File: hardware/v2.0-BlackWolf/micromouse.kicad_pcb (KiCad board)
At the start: 2 copper layers, 100 x 74 mm, 106 parts, among them CN1 7_PIN_HEADER, CN2 5_PIN_HEADER, M1 MOTOR_MOUNTS_AND_ENCODERS, M2 LEFT_MOTOR, M3 2.54MM-SLIDE-SWITCH_TS02_SWIT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, M4 RIGHT_MOTOR, P1 B3B-PH-SM4-TB, P2 B3B-PH-SM4-TB, Q1 DMN3150LW, Q2 DMN3150LW, Q3 DMN3150LW, Q4 DMN3150LW, Q5 TEFT4300, Q6 TEFT4300, Q7 TEFT4300, Q8 TEFT4300, SW1 SWITCH_DPST, SW2 SWITCH_DPST, SW3 SWITCH_DPST, U1 STM32F446RE_LQFP64, U10 MPU-9250, U11 TPS76850, U12 TPS73633, U2 MAX14871, U3 MAX14871, U9 HCMS-2901

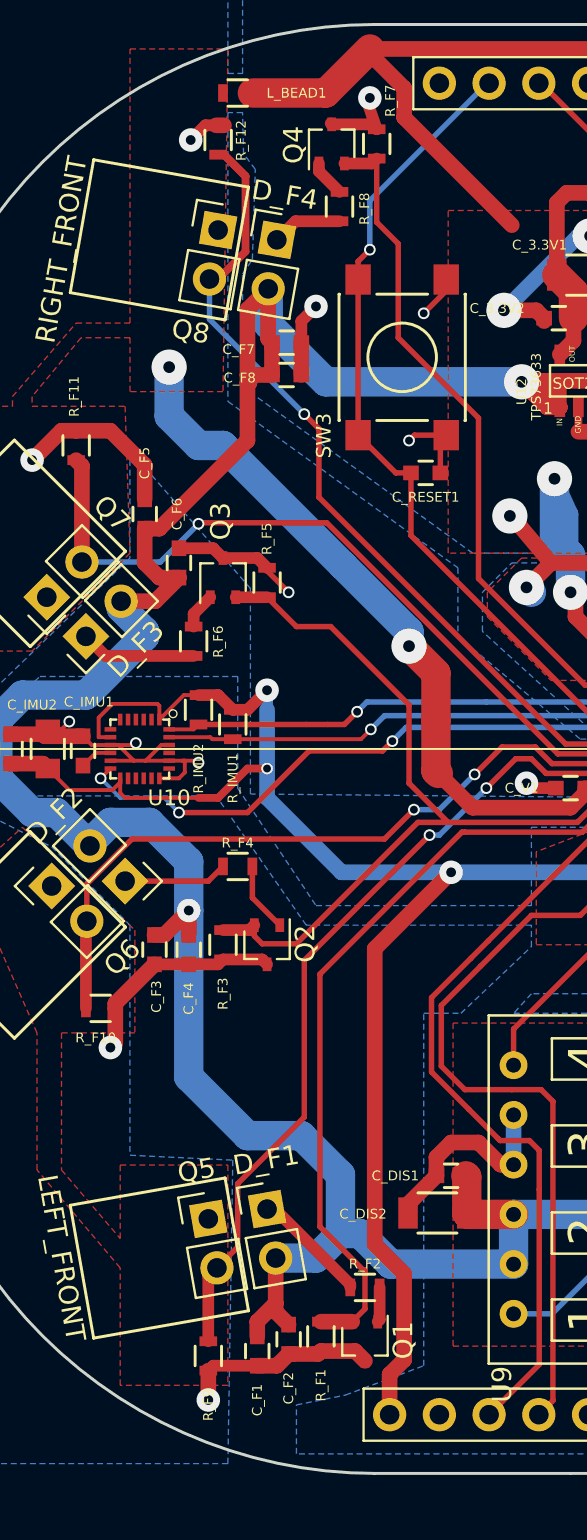
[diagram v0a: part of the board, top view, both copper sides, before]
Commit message: PCB: Fixed wrong NMOS pinmap
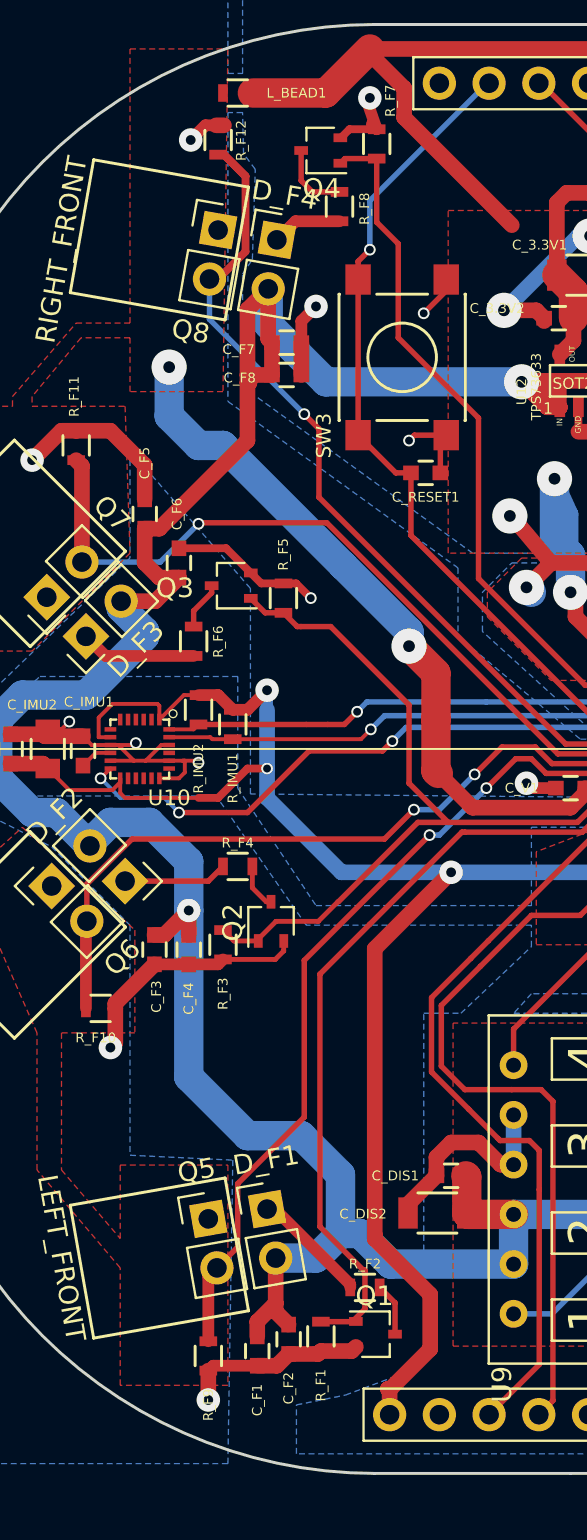
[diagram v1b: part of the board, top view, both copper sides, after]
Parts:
- R_F4, R_F6: value 10 -> 20
- moved Q2 1.21 mm to (155.7, 98.8), turned to 90 degrees
- moved R_F5 1.16 mm to (156.3, 82.3)
- moved Q4 0.65 mm to (158.2, 59.4), turned to 180 degrees
- moved Q1 0.65 mm to (161.0, 119.9), turned to 0 degrees
- moved Q3 0.59 mm to (153.7, 81.7), turned to 180 degrees
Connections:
- Q1 pad 1: Net-(Q1-Pad1) -> EMITTER_FL
- Q1 pad 2: EMITTER_FL -> GND
- Q1 pad 3: GND -> Net-(Q1-Pad3)
- Q2 pad 1: Net-(Q2-Pad1) -> EMITTER_SIDES
- Q2 pad 2: EMITTER_SIDES -> GND
- Q2 pad 3: GND -> Net-(Q2-Pad3)
- Q3 pad 1: Net-(Q3-Pad1) -> EMITTER_SIDES
- Q3 pad 2: EMITTER_SIDES -> GND
- Q3 pad 3: GND -> Net-(Q3-Pad3)
- Q4 pad 1: Net-(Q4-Pad1) -> EMITTER_FR
- Q4 pad 2: EMITTER_FR -> GND
- Q4 pad 3: GND -> Net-(Q4-Pad3)
- R_F2 pad 2: Net-(Q1-Pad1) -> Net-(Q1-Pad3)
- R_F4 pad 2: Net-(Q2-Pad1) -> Net-(Q2-Pad3)
- R_F6 pad 2: Net-(Q3-Pad1) -> Net-(Q3-Pad3)
- R_F8 pad 2: Net-(Q4-Pad1) -> Net-(Q4-Pad3)
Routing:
- net Net-(Q4-Pad3): track 0.00 -> 3.74 mm
- net Net-(Q2-Pad1): track 3.58 -> 0.00 mm
- net Net-(Q1-Pad3): track 0.00 -> 2.71 mm
- net Net-(Q3-Pad3): track 0.00 -> 2.47 mm
- net Net-(Q2-Pad3): track 0.00 -> 2.34 mm
- net GND: track 459.3 -> 461.2 mm
- net Net-(Q4-Pad1): track 1.88 -> 0.00 mm
- net Net-(Q3-Pad1): track 1.85 -> 0.00 mm
- net Net-(Q1-Pad1): track 1.79 -> 0.00 mm
- net EMITTER_SIDES: track 42.8 -> 41.4 mm
- net +3V3: track 286.7 -> 288.1 mm

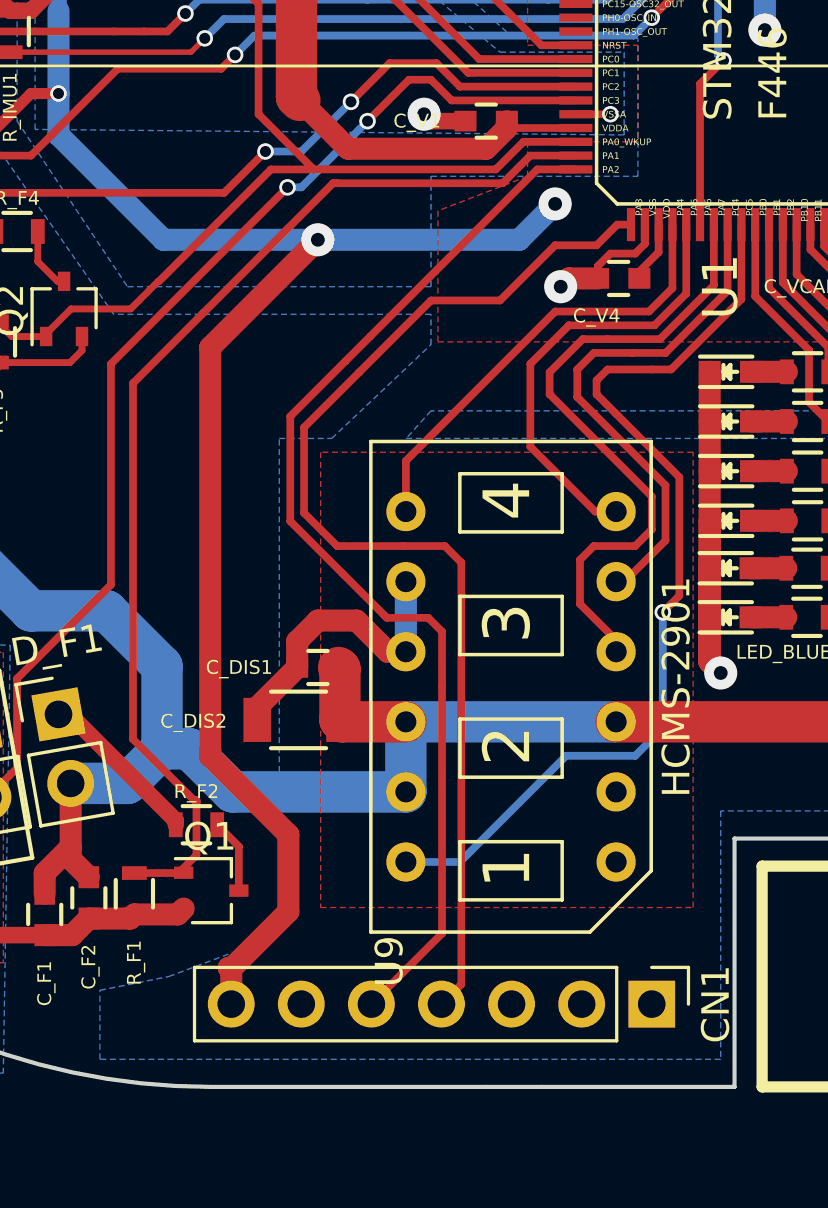
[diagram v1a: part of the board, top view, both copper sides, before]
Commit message: PCB: Fixed UART pins
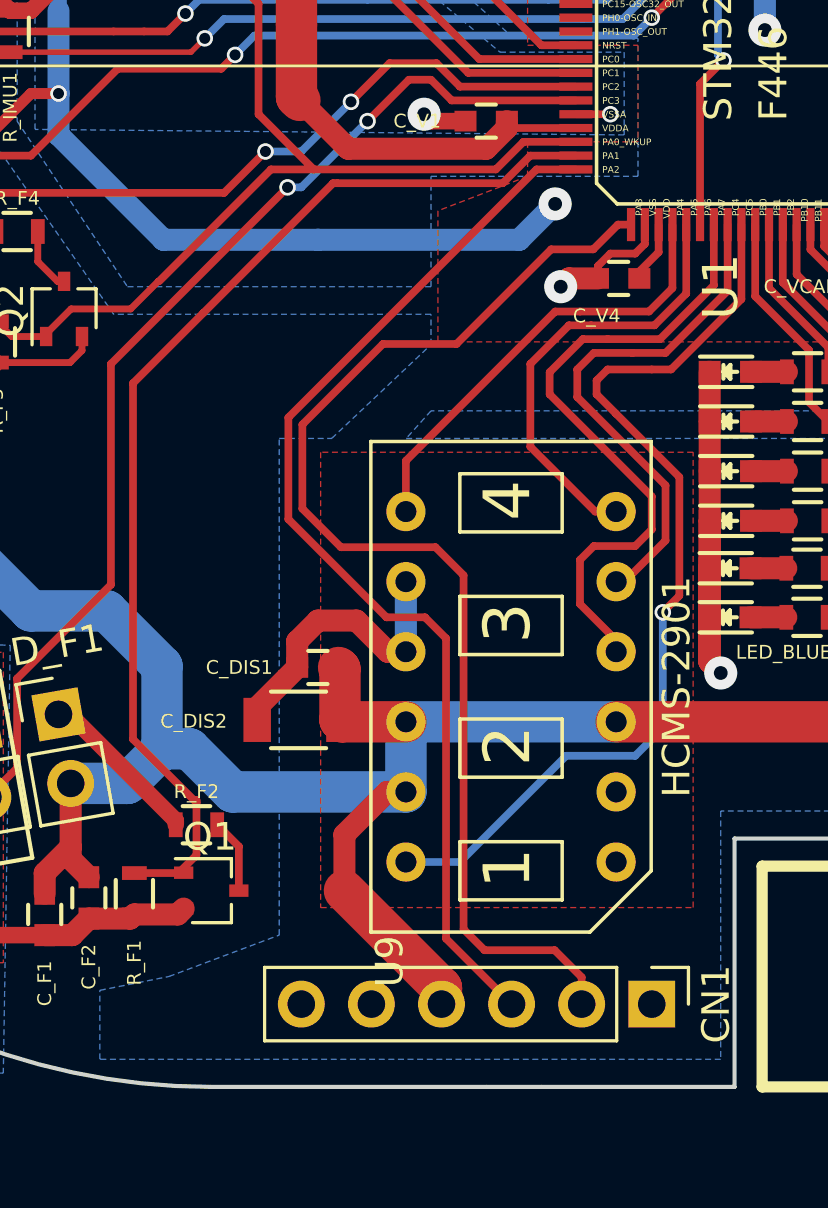
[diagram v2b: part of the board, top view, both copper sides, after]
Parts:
- CN1: value 7_PIN_HEADER -> 6_PIN_HEADER; footprint Pin_Headers:Pin_Header_Straight_1x07_Pitch2.54mm -> Pin_Headers:Pin_Header_Straight_1x06_Pitch2.54mm
- CN2: value 5_PIN_HEADER -> 6_PIN_HEADER
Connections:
- CN1 pad 1: GND -> Net-(CN1-Pad1)
- CN1 pad 2: Net-(CN1-Pad2) -> USART_RX
- CN1 pad 3: Net-(CN1-Pad3) -> USART_TX
- CN1 pad 4: USART_RX -> +5V
- CN1 pad 5: USART_TX -> Net-(CN1-Pad5)
- CN1 pad 6: Net-(CN1-Pad6) -> GND
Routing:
- net +3V3: track 288.1 -> 256.5 mm, vias 12 -> 11
- net +5V: track 206.4 -> 221.8 mm
- net USART_RX: track 40.7 -> 43.6 mm

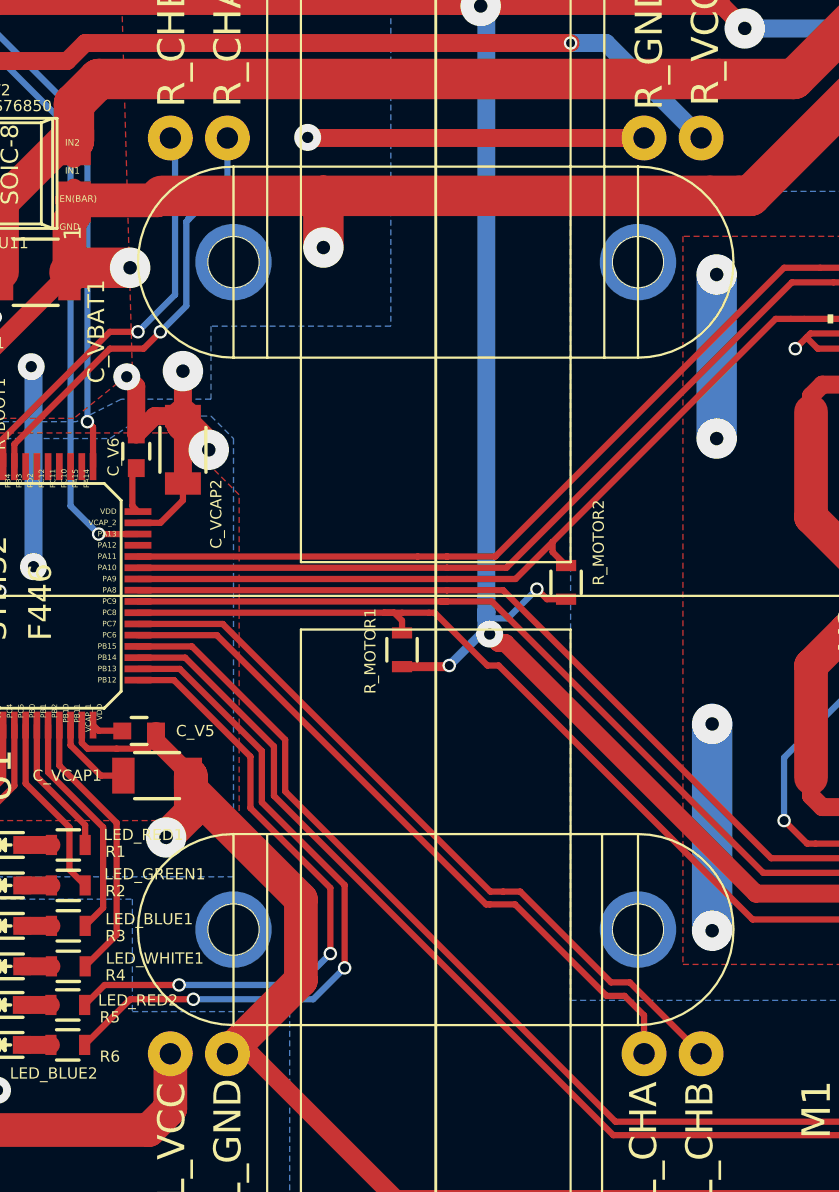
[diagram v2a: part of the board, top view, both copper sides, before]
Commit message: PCB: Fixed floating PWM output problem
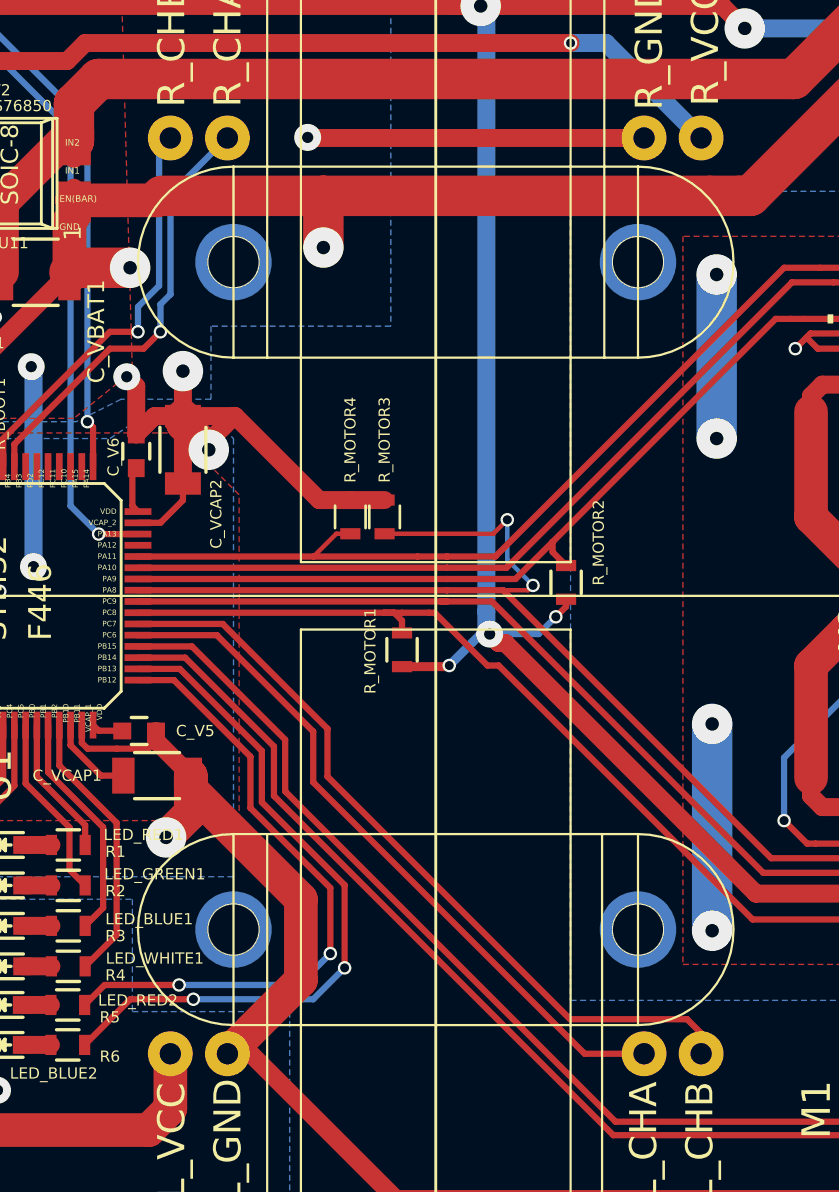
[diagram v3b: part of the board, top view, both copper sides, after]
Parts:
- added R_MOTOR3: 10k, Resistors_SMD:R_0603, F.Cu at (196.7, 86.5)
- added R_MOTOR4: 10k, Resistors_SMD:R_0603, F.Cu at (195.2, 86.5)
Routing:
- net GND: track 461.2 -> 473.7 mm
- net MOTOR_L_PWM: track 36.9 -> 47.4 mm, vias 0 -> 2
- net MOTOR_R_PWM: track 50.5 -> 52.6 mm
- net ROT_L_CHB: track 33.0 -> 34.8 mm

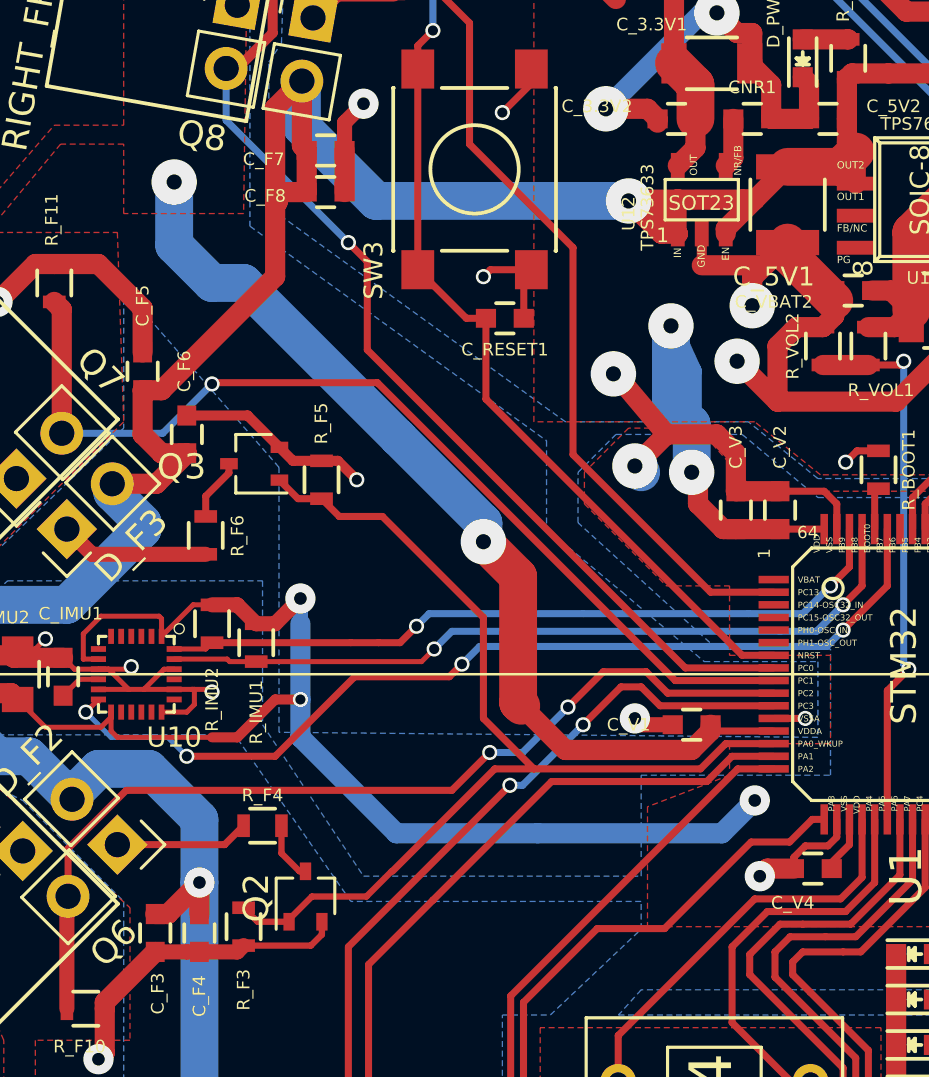
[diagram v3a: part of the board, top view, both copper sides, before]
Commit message: PCB: Added IR LED switch line
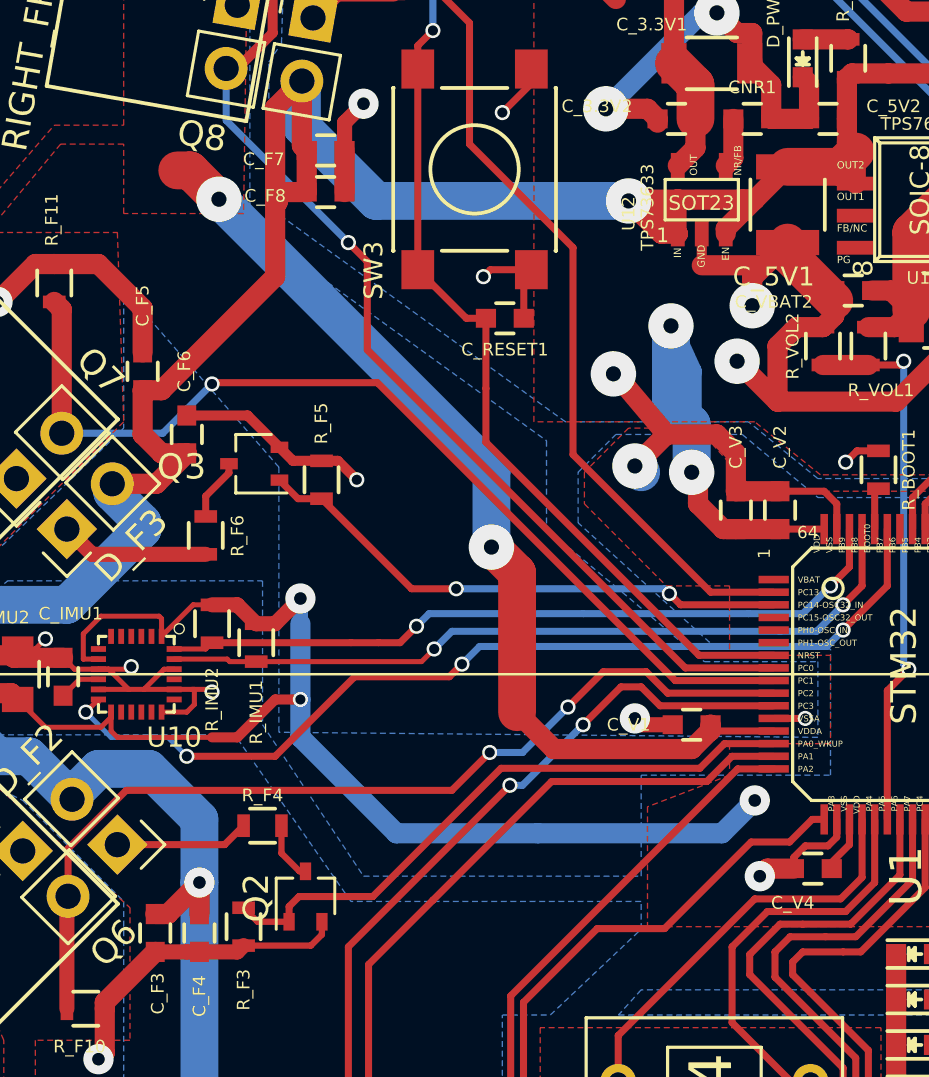
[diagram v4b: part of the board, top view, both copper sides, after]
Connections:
- Q2 pad 1: EMITTER_SIDES -> EMITTER_L
- Q3 pad 1: EMITTER_SIDES -> EMITTER_R
- R_F3 pad 1: EMITTER_SIDES -> EMITTER_L
- R_F5 pad 1: EMITTER_SIDES -> EMITTER_R
- U1 pad PA0_: EMITTER_SIDES -> EMITTER_L
- U1 pad PC14: Net-(U1-PadPC14) -> EMITTER_R
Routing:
- net EMITTER_SIDES: track 41.4 -> 0.00 mm
- net EMITTER_L: track 0.00 -> 24.6 mm
- net EMITTER_R: track 0.00 -> 21.6 mm, vias 0 -> 2
- net RESET: track 43.1 -> 44.1 mm
